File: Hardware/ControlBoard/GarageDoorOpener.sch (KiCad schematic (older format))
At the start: 48 parts, among them J1 Conn_01x04, J2 RJ45, Q1 DMG1012T-7, U1 Argon/Boron, U2 TPS56637, U3 CPC1002N, U4 VL53L1X

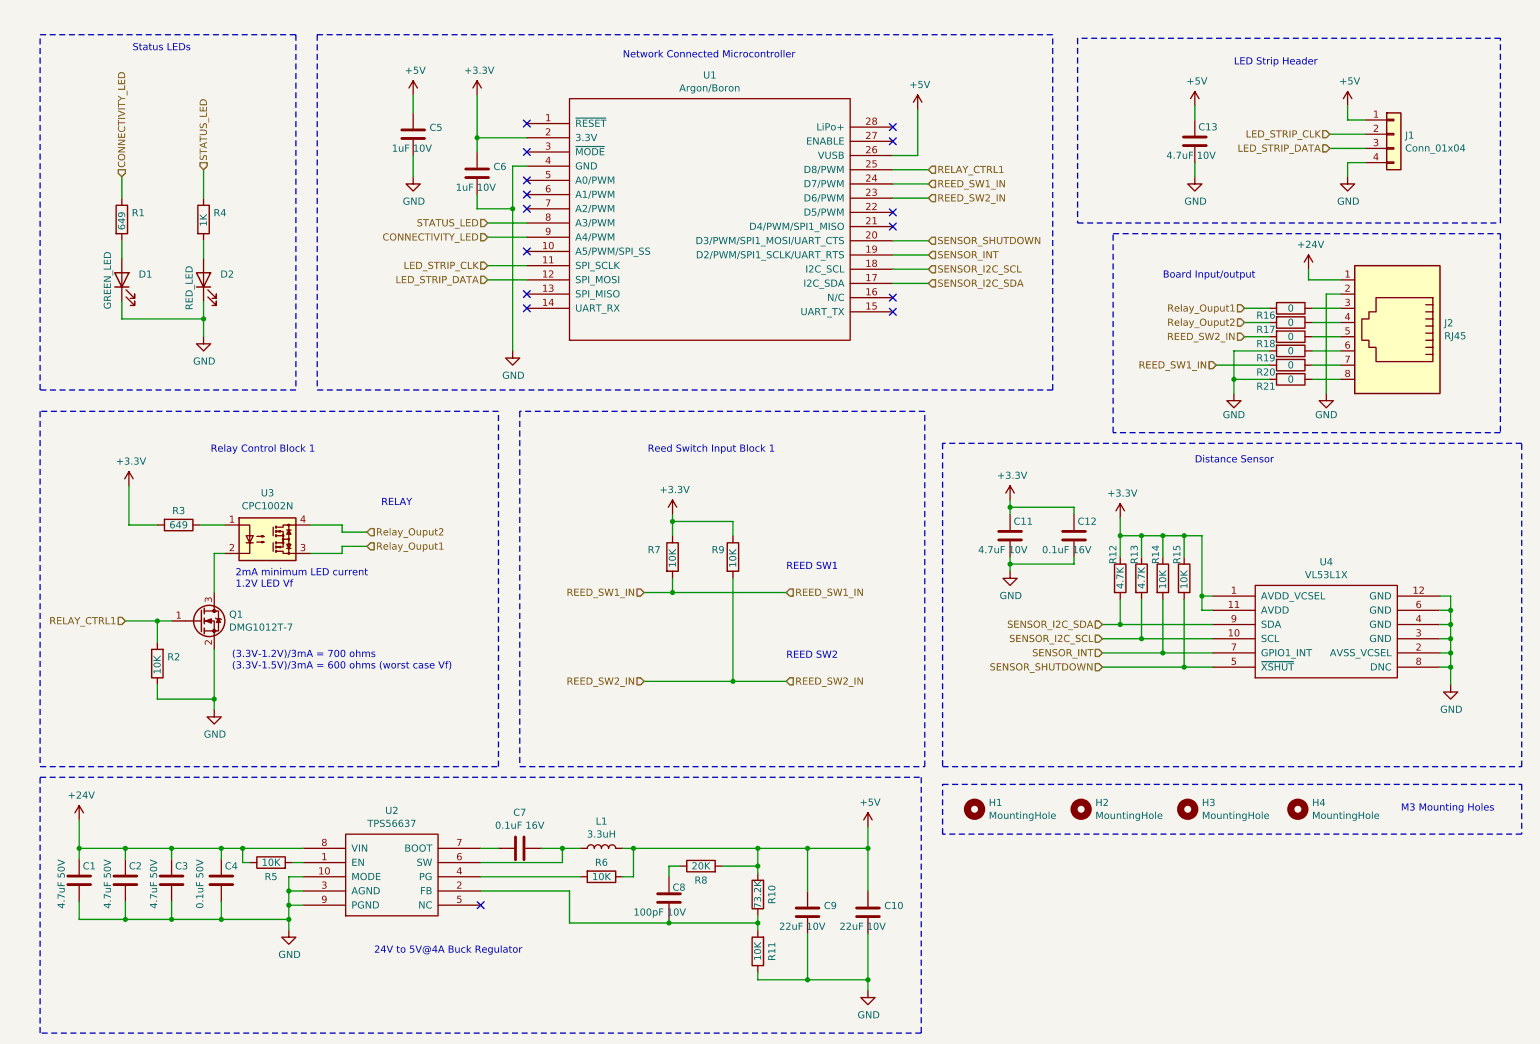
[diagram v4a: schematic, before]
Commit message: added some bits to the schematic, BoM updated
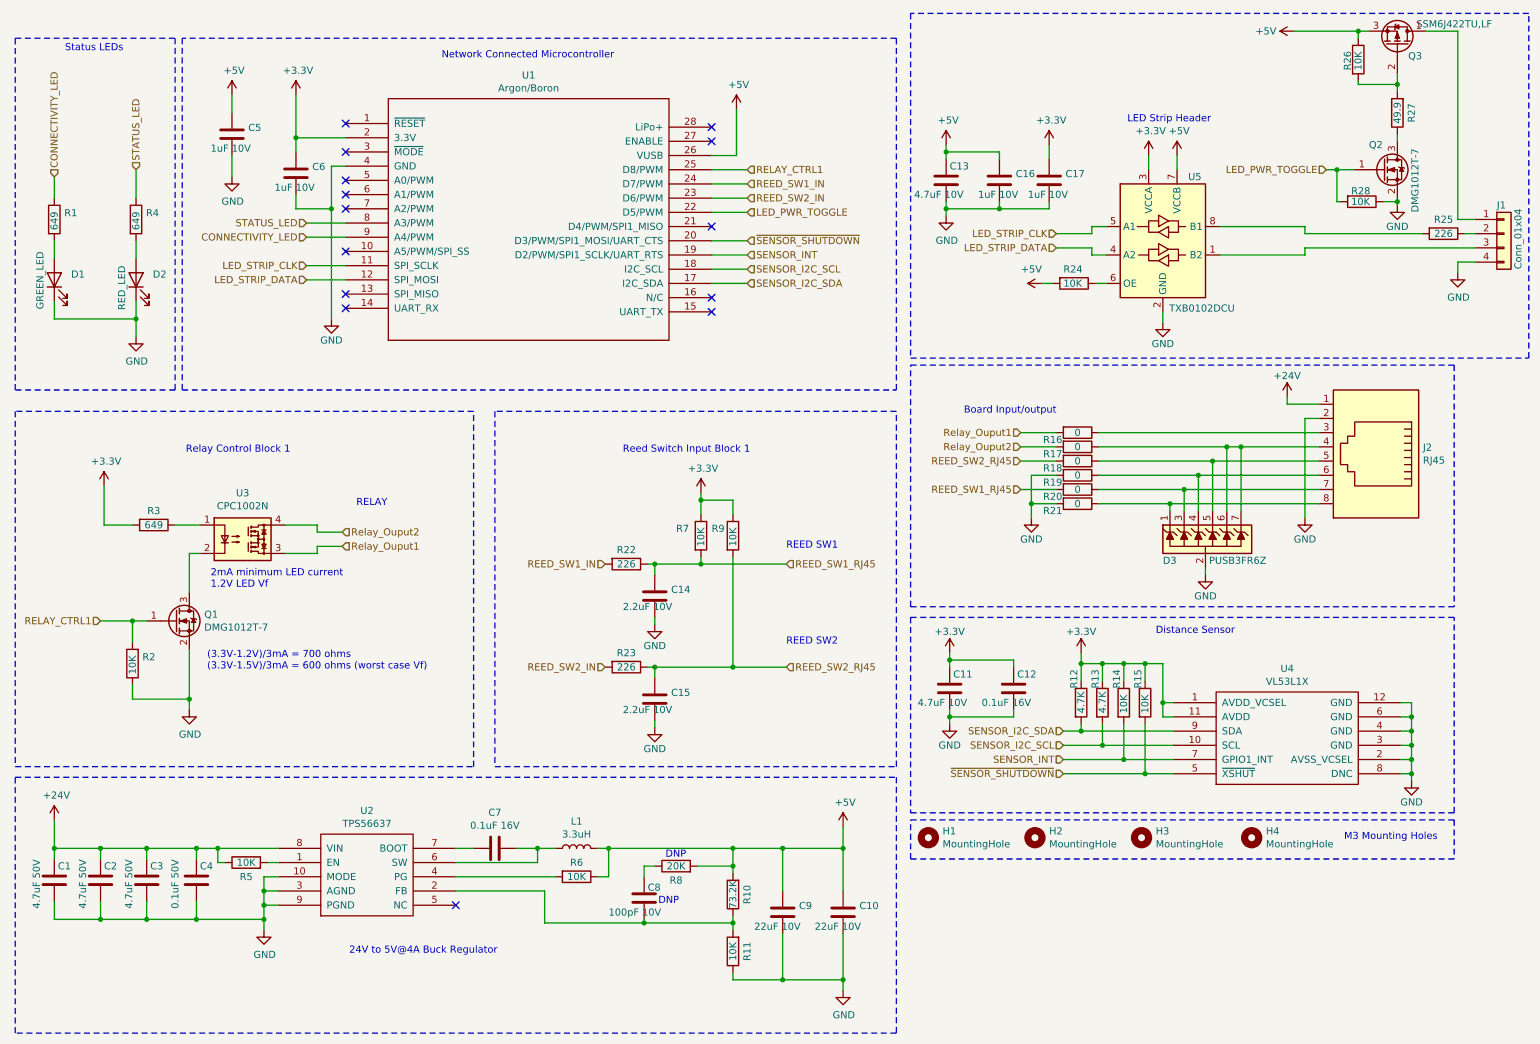
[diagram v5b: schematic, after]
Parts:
- added C14, C15: 2.2uF 10V, Capacitor_SMD:C_0603_1608Metric, symbol Device:C
- added C16, C17: 1uF 10V, Capacitor_SMD:C_0603_1608Metric, symbol Device:C
- added D3: PUSB3FR6Z, Global_Parts:Nexperia_XSON7, symbol Global_Parts:PUSB3FR6Z
- added Q2: DMG1012T-7, Package_TO_SOT_SMD:SOT-523, symbol Device:Q_NMOS_GSD
- added Q3: SSM6J422TU,LF, Package_TO_SOT_SMD:SOT-23, symbol device:Q_PMOS_DGS
- added R22, R23, R25: 226, Resistor_SMD:R_0603_1608Metric, symbol device:R
- added R24, R26, R28: 10K, Resistor_SMD:R_0603_1608Metric, symbol Device:R
- added R27: 49.9, Resistor_SMD:R_0603_1608Metric, symbol device:R
- added U5: TXB0102DCU, Package_SO:VSSOP-8_2.4x2.1mm_P0.5mm, symbol Logic_LevelTranslator:TXB0102DCU
- R4: value 1K -> 649
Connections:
- net +3V3: now also C17.1, U5.3 (VCCA)
- net +5V: now also C16.1, Q3.3 (S), R24.2, R26.1, U5.7 (VCCB); no longer J1.1 (Pin_1)
- net GND: now also C14.2, C15.2, C16.2, C17.2, D3.2 (A), Q2.2 (S), R28.1, U5.2 (GND)
- net LED_STRIP_CLK: now also U5.5 (A1); no longer J1.2 (Pin_2)
- net LED_STRIP_DATA: now also U5.4 (A2); no longer J1.3 (Pin_3)
- net REED_SW1_IN: now also R22.2; no longer R20.2, R7.2
- net REED_SW2_IN: now also R23.2; no longer R18.2, R9.2
- net LED_PWR_TOGGLE: now reaches U1.22 (D5/PWM)
- net LED_PWR_TOGGLE: now also Q2.1 (G), R28.2
- net at J2.8, R21.1: now also D3.1 (K)
- net at J2.7, R20.1: now also D3.3 (K)
- net at J2.6, R19.1: now also D3.4 (K)
- net at J2.5, R18.1: now also D3.5 (K)
- net at J2.4, R17.1: now also D3.6 (K), D3.7 (K)
- net SENSOR_SHUTDOWN renamed ~SENSOR_SHUTDOWN
- new net: J1.1 (Pin_1), Q3.1 (D)
- new net: J1.2 (Pin_2), R25.1
- new net: J1.3 (Pin_3), U5.1 (B2)
- new net: R24.1, U5.6 (OE)
- new net: R25.2, U5.8 (B1)
- new net: Q3.2 (G), R26.2, R27.2
- new net: Q2.3 (D), R27.1
- new net REED_SW1_RJ45: C14.1, R20.2, R22.1, R7.2
- new net REED_SW2_RJ45: C15.1, R18.2, R23.1, R9.2
- no-connect marks 15 -> 14
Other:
- note added: "DNP"
- moved on the sheet: C1, C10, C11, C12, C13, C2, C3, C4, C5, C6, C7, C8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

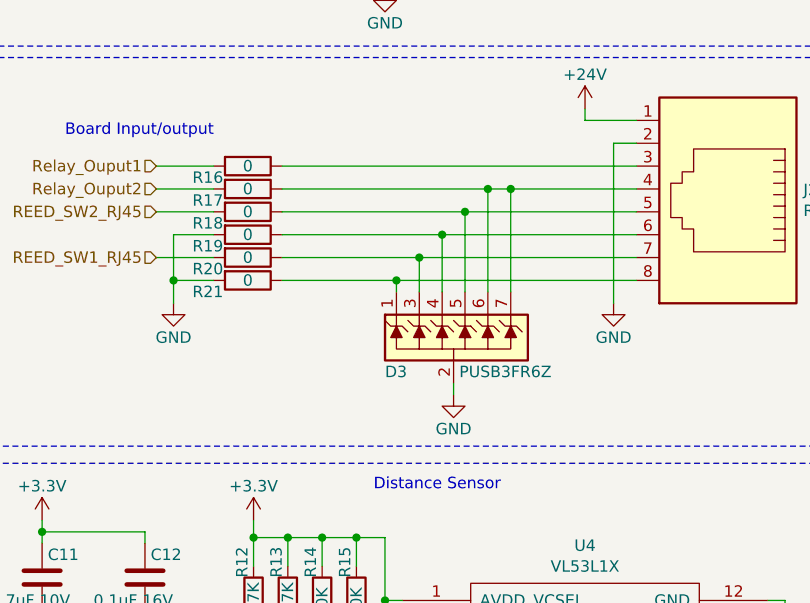
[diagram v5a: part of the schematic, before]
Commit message: finished the control board, ordered PCBs!
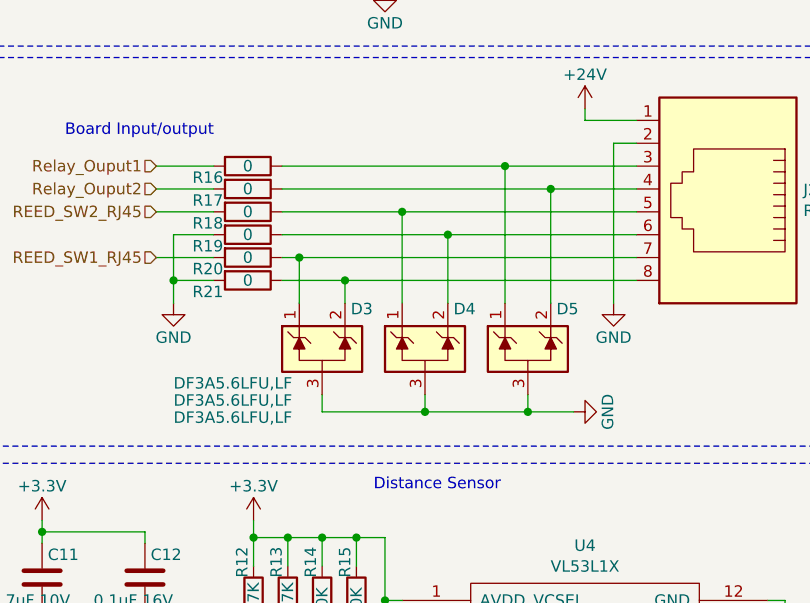
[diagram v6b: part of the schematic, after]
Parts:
- removed D3: PUSB3FR6Z, Global_Parts:Nexperia_XSON7, symbol Global_Parts:PUSB3FR6Z
- added D3, D4, D5: DF3A5.6LFU,LF, Package_TO_SOT_SMD:SOT-323_SC-70, symbol Global_Parts:DF3A5.6LFU,LF
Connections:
- net GND: now also D3.3 (A), D4.3 (A), D5.3 (A)
- net at J2.8, R21.1: now also D3.2 (K)
- net at J2.7, R20.1: now also D3.1 (K)
- net at J2.6, R19.1: now also D4.2 (K)
- net at J2.5, R18.1: now also D4.1 (K)
- net at J2.4, R17.1: now also D5.2 (K)
- net at J2.3, R16.1: now also D5.1 (K)
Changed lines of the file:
@@
 Title "Garage Door Opener"
 Date "2020-05-02"
-Rev "1b"
+Rev "1c"
 Comp "Martian Engineering"
 Comment1 "Designer: Matthew Glazer"
@@
 Wire Notes Line
 	6825 3025 10650 3025
-Wire Wire Line
-	8150 4000 8650 4000
-Wire Wire Line
-	9700 3900 8750 3900
-Wire Wire Line
-	8150 3800 8850 3800
-Wire Wire Line
-	8150 3600 9050 3600
-Wire Wire Line
-	9700 3500 8150 3500
 $Comp
 L Device:R R?
@@
 	8600 2650 8600 2725
 $Comp
-L Global_Parts:PUSB3FR6Z D3
-U 1 1 5EE102C3
-P 8950 4250
-F 0 "D3" H 8600 4100 50  0000 L CNN
-F 1 "PUSB3FR6Z" H 8925 4100 50  0000 L CNN
-F 2 "Global_Parts:Nexperia_XSON7" H 9250 4200 50  0001 L CNN
-F 3 "http://www.littelfuse.com/~/media/files/littelfuse/technical%20resources/documents/data%20sheets/sp05xxba.pdf" H 9075 4375 50  0001 C CNN
-	1    8950 4250
-	1    0    0    -1
-$EndComp
-$Comp
 L power:GND #PWR029
 U 1 1 5EFA799B
-P 8900 4500
+P 9425 4575
 AR Path="/5EFA799B" Ref="#PWR029"  Part="1"
 AR Path="/5EB107FD/5EFA799B" Ref="#PWR?"  Part="1"
-F 0 "#PWR029" H 8900 4250 50  0001 C CNN
-F 1 "GND" H 8900 4350 50  0000 C CNN
-F 2 "" H 8900 4500 50  0001 C CNN
-F 3 "" H 8900 4500 50  0001 C CNN
-	1    8900 4500
-	1    0    0    -1
-$EndComp
-Wire Wire Line
-	8900 4500 8900 4450
-Wire Wire Line
-	8650 4050 8650 4000
-Connection ~ 8650 4000
-Wire Wire Line
-	8650 4000 9700 4000
-Wire Wire Line
-	8750 4050 8750 3900
-Connection ~ 8750 3900
-Wire Wire Line
-	8750 3900 8150 3900
-Wire Wire Line
-	8850 4050 8850 3800
-Connection ~ 8850 3800
-Wire Wire Line
-	8850 3800 9700 3800
-Wire Wire Line
-	9700 3700 8950 3700
-Wire Wire Line
-	8950 4050 8950 3700
-Connection ~ 8950 3700
-Wire Wire Line
-	8950 3700 8150 3700
-Wire Wire Line
-	9050 4050 9050 3600
-Connection ~ 9050 3600
-Wire Wire Line
-	9050 3600 9150 3600
-Wire Wire Line
-	9150 4050 9150 3600
-Connection ~ 9150 3600
-Wire Wire Line
-	9150 3600 9700 3600
+F 0 "#PWR029" H 9425 4325 50  0001 C CNN
+F 1 "GND" H 9425 4425 50  0000 C CNN
+F 2 "" H 9425 4575 50  0001 C CNN
+F 3 "" H 9425 4575 50  0001 C CNN
+	1    9425 4575
+	0    -1   -1   0
+$EndComp
 $Comp
 L Device:Q_NMOS_GSD Q2
@@
 Wire Wire Line
 	5675 1950 5425 1950
+$Comp
+L Global_Parts:DF3A5.6LFU,LF D3
+U 1 1 5ECCA6ED
+P 8325 4300
+F 0 "D3" H 8450 4475 50  0000 L CNN
+F 1 "DF3A5.6LFU,LF" H 7675 4150 50  0000 L CNN
+F 2 "Package_TO_SOT_SMD:SOT-323_SC-70" H 8550 4250 50  0001 L CNN
+F 3 "http://www.littelfuse.com/~/media/files/littelfuse/technical%20resources/documents/data%20sheets/sp05xxba.pdf" H 8450 4425 50  0001 C CNN
+	1    8325 4300
+	1    0    0    -1
+$EndComp
+$Comp
+L Global_Parts:DF3A5.6LFU,LF D4
+U 1 1 5ECDBA73
+P 8775 4300
+F 0 "D4" H 8900 4475 50  0000 L CNN
+F 1 "DF3A5.6LFU,LF" H 7675 4075 50  0000 L CNN
+F 2 "Package_TO_SOT_SMD:SOT-323_SC-70" H 9000 4250 50  0001 L CNN
+F 3 "http://www.littelfuse.com/~/media/files/littelfuse/technical%20resources/documents/data%20sheets/sp05xxba.pdf" H 8900 4425 50  0001 C CNN
+	1    8775 4300
+	1    0    0    -1
+$EndComp
+$Comp
+L Global_Parts:DF3A5.6LFU,LF D5
+U 1 1 5ECDBEB3
+P 9225 4300
+F 0 "D5" H 9350 4475 50  0000 L CNN
+F 1 "DF3A5.6LFU,LF" H 7675 4000 50  0000 L CNN
+F 2 "Package_TO_SOT_SMD:SOT-323_SC-70" H 9450 4250 50  0001 L CNN
+F 3 "http://www.littelfuse.com/~/media/files/littelfuse/technical%20resources/documents/data%20sheets/sp05xxba.pdf" H 9350 4425 50  0001 C CNN
+	1    9225 4300
+	1    0    0    -1
+$EndComp
+Wire Wire Line
+	8325 4575 8325 4500
+Wire Wire Line
+	8325 4575 8775 4575
+Wire Wire Line
+	8775 4500 8775 4575
+Connection ~ 8775 4575
+Wire Wire Line
+	8775 4575 9225 4575
+Wire Wire Line
+	9225 4575 9225 4500
+Connection ~ 9225 4575
+Wire Wire Line
+	9225 4575 9425 4575
+Wire Wire Line
+	8150 4000 8425 4000
+Wire Wire Line
+	8150 3900 8225 3900
+Wire Wire Line
+	8425 4100 8425 4000
+Connection ~ 8425 4000
+Wire Wire Line
+	8425 4000 9700 4000
+Wire Wire Line
+	8225 4100 8225 3900
+Connection ~ 8225 3900
+Wire Wire Line
+	8225 3900 9700 3900
+Wire Wire Line
+	8150 3700 8675 3700
+Wire Wire Line
+	8150 3800 8875 3800
+Wire Wire Line
+	8675 4100 8675 3700
+Connection ~ 8675 3700
+Wire Wire Line
+	8675 3700 9700 3700
+Wire Wire Line
+	8875 4100 8875 3800
+Connection ~ 8875 3800
+Wire Wire Line
+	8875 3800 9700 3800
+Wire Wire Line
+	8150 3600 9325 3600
+Wire Wire Line
+	8150 3500 9125 3500
+Wire Wire Line
+	9125 4100 9125 3500
+Connection ~ 9125 3500
+Wire Wire Line
+	9125 3500 9700 3500
+Wire Wire Line
+	9325 4100 9325 3600
+Connection ~ 9325 3600
+Wire Wire Line
+	9325 3600 9700 3600
 $EndSCHEMATC
